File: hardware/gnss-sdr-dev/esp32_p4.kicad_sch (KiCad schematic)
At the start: 59 parts, among them U6 ESP32-P4NRW32X, U7 W25Q128JVYIQ, U8 TLV62569DRLR, U9 TPS62152RGTR, Y1 ECS-400-10-37B2-CKY-TR

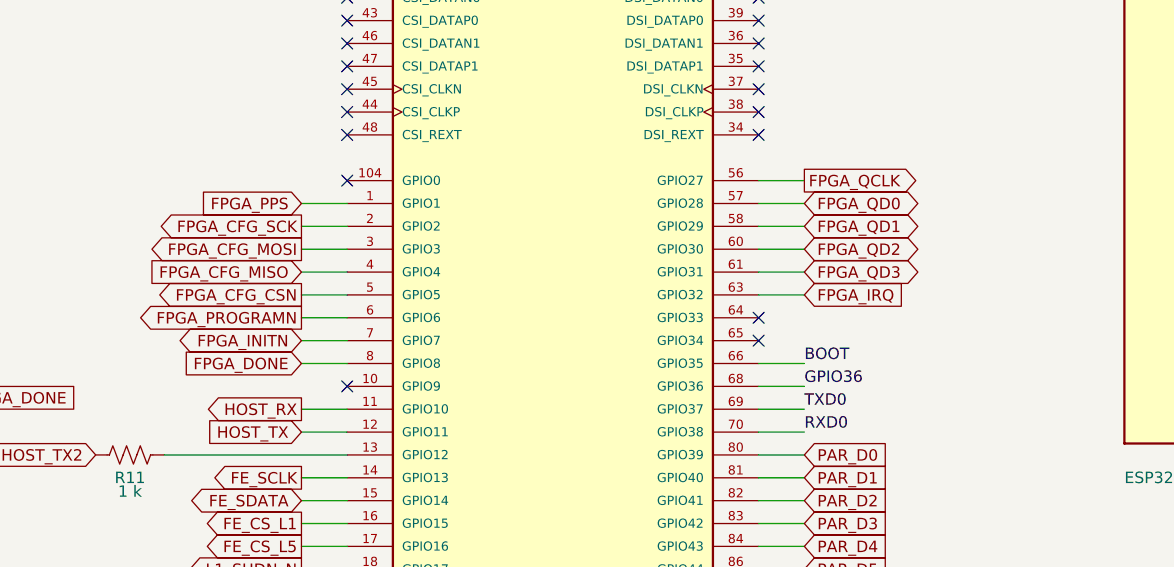
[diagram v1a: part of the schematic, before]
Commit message: hardware(gnss-sdr-dev): the rest of the board routed except the P4's new pins, and the Mantis flight-data NAND added -- FPGA fanout and supplies, sample lines and clock, power entry, IMU, USB-HS connector side; silkscreen references hidden
Silkscreen:
- Reference designators hidden on every part, the new ones included.

Flight-data flash (new sheet "Data flash", flash.kicad_sch):
- U701 is the Mantis U11 part and footprint, GD5F2GQ5UEYIGR (2 Gbit SPI NAND, WSON-8 8x6).
- R701 pulls CS up through reset and boot. R702/R703 pull HOLD#/WP# up, as on the Mantis. C701 is 100 nF.
- It uses the P4's four free GPIOs: GPIO0 = CS, GPIO9 = MISO, GPIO33 = SCK, GPIO34 = MOSI.
  - GPIO34 is the P4's JTAG-source strap, so it only drives the NAND's input and has no pull.
- ERC: 0 errors. The two new warnings are pin-type warnings like those already on the sheet.
- Placed east of the P4 at (147.6, 139). Its locals are routed; its P4 links are not (see below).

Rules:
- New 0.1 mm clearance inside U501's courtyard (0.8 mm BGA), written like the fine-pitch rule for U6/U7/U9/U10.
- Zone fills keep the board default.

Planes:
- +3V3_MCU plane on In4 over the digital side.
- +1V1_FPGA island on B.Cu: the ball field, a finger to each core decoupler, and a strip east of R501-R512 down to the 1.1 V buck.

FPGA:
- Via-in-pad on every supply, ground and interior signal ball.
- Fixed escape lanes run between the ball columns below and south-west of the field.
- Routed:
  - 1.1 V, 2.5 V (on In4, along the east edge) and VCCAUX.
  - The eight sample lines from the shield's escape vias, with their DNP edge-rate shunts.
  - The 27 MHz sample clock out of the shield.
  - Logic-analyzer header (13 of 14 lines), JTAG, status LEDs, config flash and its pull-ups.
  - The CFG_0/1/2 mode straps, on B.Cu under the strap resistors.

Power entry and the west:
- Battery/host connector, input filter, VSS/VSYS/+BATT, VIN to the GNSS LDO and on to the P4 buck's filter.
- GNSS LDO output, +3V3_GNSS and +1V8_LNA, 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
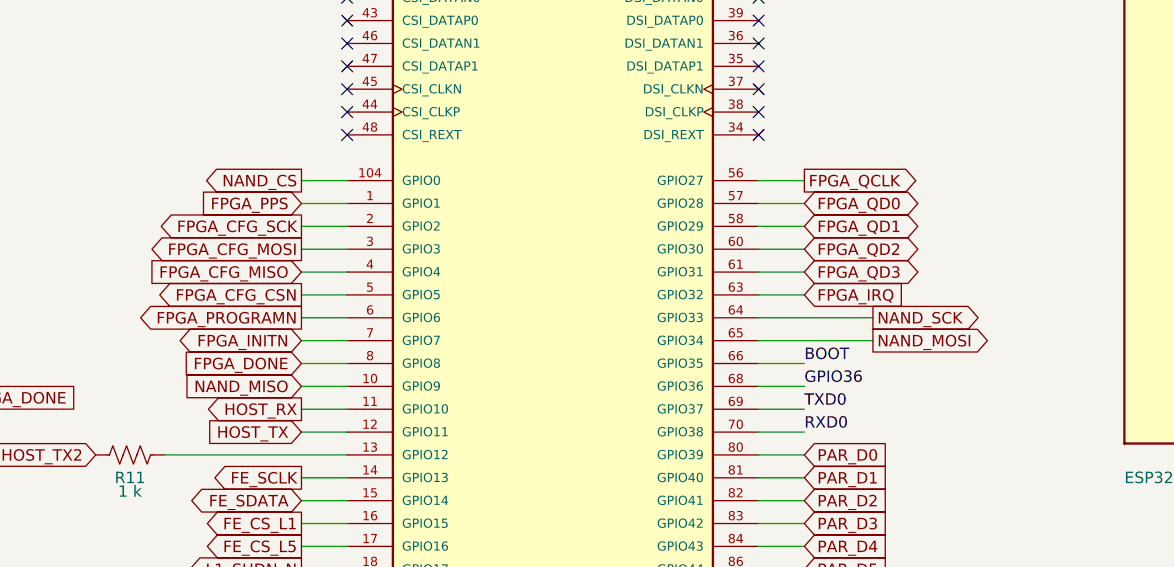
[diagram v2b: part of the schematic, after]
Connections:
- net NAND_MISO: now reaches U6.10 (GPIO9)
- net NAND_CS: now reaches U6.104 (GPIO0)
- net NAND_SCK: now reaches U6.64 (GPIO33)
- net NAND_MOSI: now reaches U6.65 (GPIO34)
- no-connect marks 20 -> 16
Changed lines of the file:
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@@
 	)
 	(no_connect
-		(at 78.74 153.67)
-	)
-	(no_connect
 		(at 124.46 118.11)
 	)
 	(no_connect
-		(at 124.46 146.05)
-	)
-	(no_connect
-		(at 124.46 148.59)
-	)
-	(no_connect
 		(at 124.46 125.73)
 	)
@@
 	)
 	(no_connect
-		(at 78.74 130.81)
-	)
-	(no_connect
 		(at 78.74 115.57)
 	)
@@
 			(hide yes)
 			(show_name no)
+			(do_not_autoplace no)
+			(effects
+				(font
+					(size 1.27 1.27)
+				)
+				(justify left)
+			)
+		)
+	)
+	(wire
+		(pts
+			(xy 78.74 130.81) (xy 73.66 130.81)
+		)
+		(stroke
+			(width 0)
+			(type default)
+		)
+	)
+	(global_label "NAND_CS"
+		(shape output)
+		(at 73.66 130.81 180)
+		(fields_autoplaced yes)
+		(effects
+			(font
+				(size 1.27 1.27)
+			)
+			(justify right)
+		)
+		(property "Intersheetrefs" "${INTERSHEET_REFS}"
+			(at 73.66 130.81 0)
+			(hide yes)
+			(show_name no)
+			(do_not_autoplace no)
+			(effects
+				(font
+					(size 1.27 1.27)
+				)
+				(justify right)
+			)
+		)
+	)
+	(wire
+		(pts
+			(xy 78.74 153.67) (xy 73.66 153.67)
+		)
+		(stroke
+			(width 0)
+			(type default)
+		)
+	)
+	(global_label "NAND_MISO"
+		(shape input)
+		(at 73.66 153.67 180)
+		(fields_autoplaced yes)
+		(effects
+			(font
+				(size 1.27 1.27)
+			)
+			(justify right)
+		)
+		(property "Intersheetrefs" "${INTERSHEET_REFS}"
+			(at 73.66 153.67 0)
+			(hide yes)
+			(show_name no)
+			(do_not_autoplace no)
+			(effects
+				(font
+					(size 1.27 1.27)
+				)
+				(justify right)
+			)
+		)
+	)
+	(wire
+		(pts
+			(xy 124.46 146.05) (xy 137.16 146.05)
+		)
+		(stroke
+			(width 0)
+			(type default)
+		)
+	)
+	(global_label "NAND_SCK"
+		(shape output)
+		(at 137.16 146.05 0)
+		(fields_autoplaced yes)
+		(effects
+			(font
+				(size 1.27 1.27)
+			)
+			(justify left)
+		)
+		(property "Intersheetrefs" "${INTERSHEET_REFS}"
+			(at 137.16 146.05 0)
+			(hide yes)
+			(show_name no)
+			(do_not_autoplace no)
+			(effects
+				(font
+					(size 1.27 1.27)
+				)
+				(justify left)
+			)
+		)
+	)
+	(wire
+		(pts
+			(xy 124.46 148.59) (xy 137.16 148.59)
+		)
+		(stroke
+			(width 0)
+			(type default)
+		)
+	)
+	(global_label "NAND_MOSI"
+		(shape output)
+		(at 137.16 148.59 0)
+		(fields_autoplaced yes)
+		(effects
+			(font
+				(size 1.27 1.27)
+			)
+			(justify left)
+		)
+		(property "Intersheetrefs" "${INTERSHEET_REFS}"
+			(at 137.16 148.59 0)
+			(hide yes)
+			(show_name no)

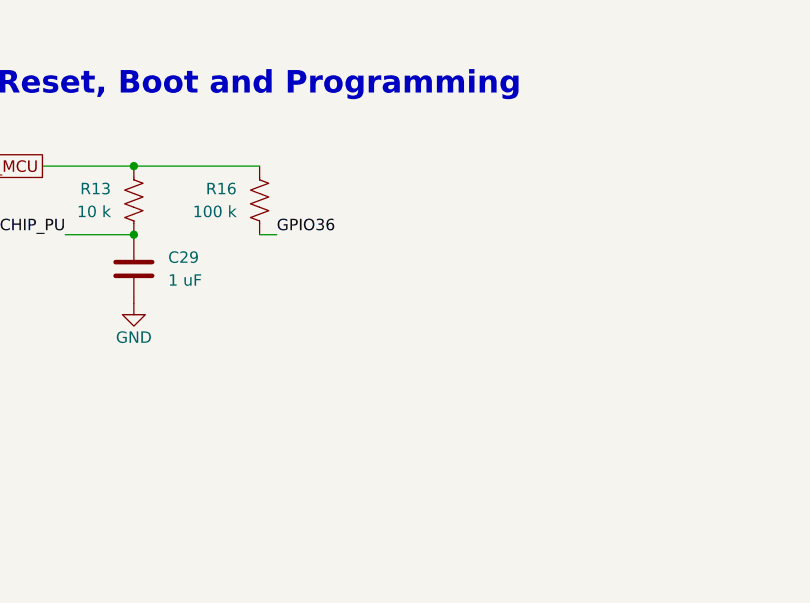
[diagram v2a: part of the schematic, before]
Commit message: hardware(gnss-sdr-dev): eight layers with the P4 wired, a boot button on GPIO35, Mantis design rules, a review pass, 3D models for every part, and the USB-HS pairs re-routed to 90 ohm
Stackup and routing:
- Eight layers on the Beetle's JLC08161H-2116 stack: F signal / In1 GND / In2 signal / In3 GND / In4 power / In5 north-south / In6 east-west / B GND (+1V1 island).
- The P4 cluster is wired (FPGA link, configuration, front-end control, boot flash, NAND, IMU, USB control). With the owner's placement work, nothing is left unconnected.

Boot button (owner: "add a boot button on GPIO35 like the space bug"):
- R15 100 k pulls GPIO35 up to +3V3_MCU. R24 1 k and SW1 (R-667995) pull it to GND, as on the Space Bug.
- The owner placed the parts. It is the only netlist change in the sheets; the rest of the sheet diffs are KiCad re-saves.

Design rules = Tinker-Mantis:
- 0.1 mm net-class clearance; 0.09 mm minimum track; 0.1 mm hole clearance; 0.2 mm hole-to-hole and copper-to-edge.
- Every copper pour keeps its own 0.2 mm clearance, which is the RF lines' ground gap.

Review pass:
- U7/U502 (W25Q128JVYIQ): the vias are moved off the 0.254 mm balls to sit beside them. JLC had queried vias the size of the ball pads. No via now overlaps a ball.
- DRC fixes:
  - the NAND_SCK via that shorted C65 moved;
  - one GND via moved for clearance;
  - C71 nudged off C72's courtyard.
- Ten +3V3 pins and caps tied to the plane; the C47-C49/C67 ground island tied in.
- Vias added:
  - 163 GND return vias beside signal and power vias and at cap grounds;
  - exposed pads: U9 gets 5 vias, U401 gets 12 (both had none).
- ESP_VDD_HP necks at P4 pins 76 and 91 widened from 0.1 to 0.2-0.3 mm.
- X/Y silkscreen letters raised to the 0.8 mm minimum. Dead stubs, duplicate segments and an overlap removed.

3D models:
- KiCad 10 does not ship models for:
  - the TQFN-28 front ends (U201/U301);
  - the TG2520SMN TCXO (Y201);
  - the Laird BMI-S-205 shield (SH1).
- They are generated with CadQuery from the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
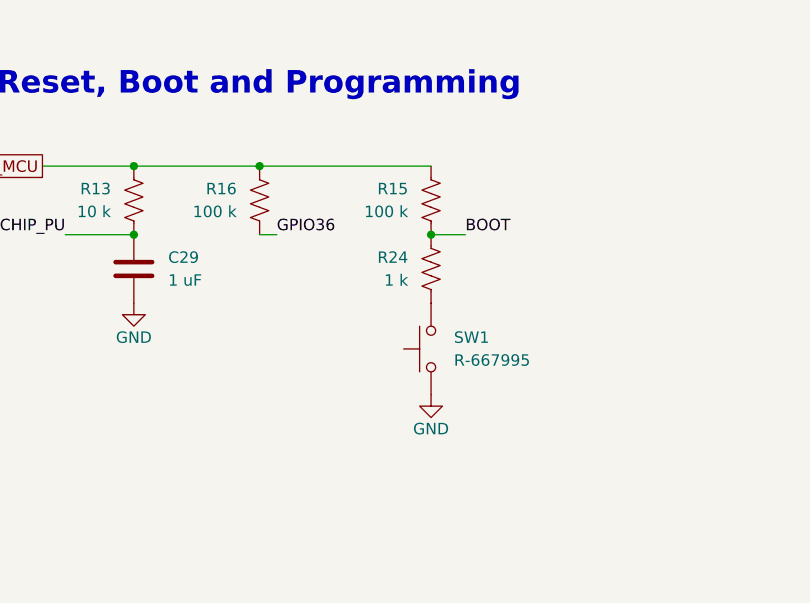
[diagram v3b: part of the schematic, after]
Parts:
- added R15: 100 k, Resistor_SMD:R_0402_1005Metric, symbol Device:R_US
- added R24: 1 k, Resistor_SMD:R_0402_1005Metric, symbol Device:R_US
- added SW1: R-667995, Footprints:R-667995_MIT, symbol Switch:SW_Push
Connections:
- net +3V3_MCU: now also R15.1
- net BOOT: now also R15.2, R24.1
- net GND: now also SW1.1
- new net: R24.2, SW1.2

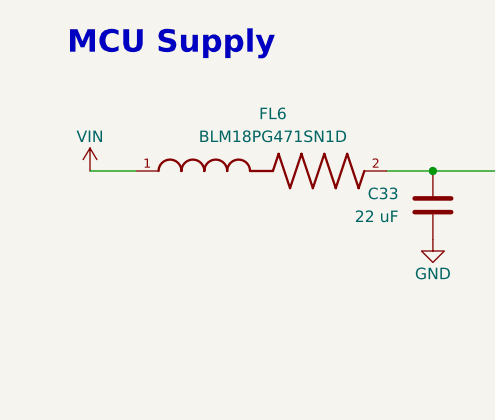
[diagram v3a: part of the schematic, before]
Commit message: hardware: the 1 uF 0402 caps consolidate on the 16 V CL05A105KO5NNNC, with the pending part and layout work
Every GRM155R61A105KE15D (Murata, 10 V X5R) becomes the Samsung CL05A105KO5NNNC (16 V X5R) on
space-bug-m8t, gnss-sdr-dev and the legacy gnss-px1105r board -- 34 symbols and their 34 footprints.
Same 0402 footprint, so only the MPN and Mfr change. The higher-rated part is already the 1 uF used
on the Tinker boards, so the BOMs now carry one 1 uF line instead of two.

Pending work committed alongside:
- space-bug-m8t: the 10 uF bulk caps go to CL21A226MOQNNNE, added CL05A106MQ5NUNC, RC0402FR-071KL and
  R-667995 parts, schematic, layout and DRC rule updates, and the new FABRICATION-NOTES.md
- gnss-sdr-dev: the 5.1 nH inductors go from LQG15HS5N1S02D to LQW15AN5N1C00D, added 1 k and 100 k
  resistors, and schematic and layout updates
- legacy gnss-px1105r: the 10 uF caps go to CL21A226MOQNNNE, plus schematic and layout updates
- tinker-beetle: the 390 pF caps go to GRM1555C1H391JA01D, the 100 k resistors to RC0402FR-07100KL,
  and the 2.2 uH inductor from XGL4020-222ME to SRP4020FA-2R2M
- gnss-sam10m8-18mm-hv: the 100 pF cap goes from CL05C101JB5NNNC to GRM1555C1H101JA01D
- the Taoglas CGGBP.25.4.A.02 antenna footprint, and project-file housekeeping

Co-Authored-By: Claude Opus 5.5 <noreply@anthropic.com>
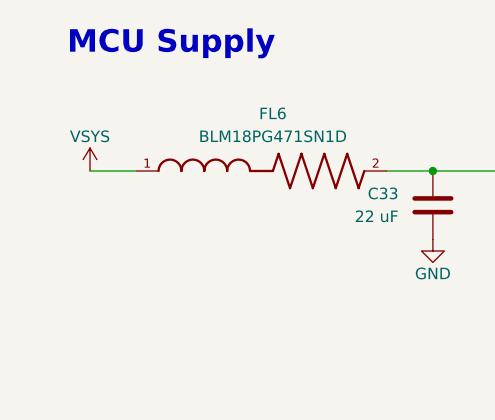
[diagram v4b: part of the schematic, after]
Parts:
- C29, C62, C63, C66, C67, C68, C69: MPN GRM155R61A105KE15D -> CL05A105KO5NNNC; Mfr Murata -> Samsung
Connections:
- net VIN renamed VSYS
